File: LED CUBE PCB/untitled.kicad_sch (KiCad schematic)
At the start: 23 parts, among them J2 Conn_01x08, J4 Conn_01x04, SW2 RESET, U1 TPS7A2633DRVR, Y3 8MHz, Y4 32.786KHz

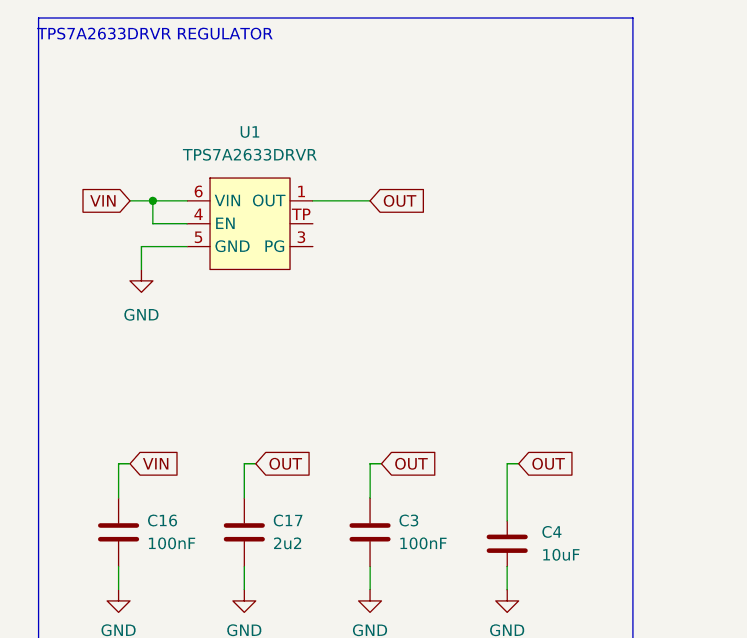
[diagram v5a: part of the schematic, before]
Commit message: Connected voltage regulator and logic level converter
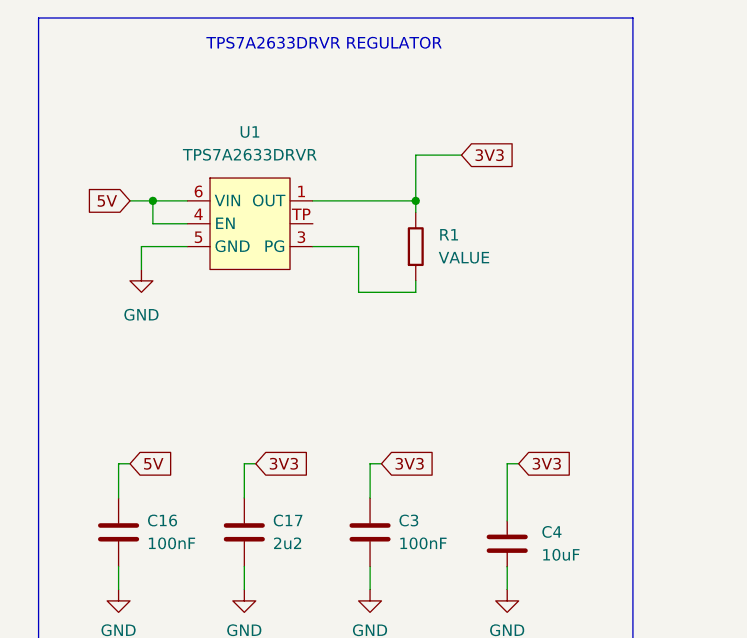
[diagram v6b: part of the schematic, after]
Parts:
- added R1: VALUE, Borna KiCAD Library:R0603, symbol Borna KiCAD Library:R0603
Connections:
- net 3V3: now also C17.1, C3.1, C4.2, U1.1 (OUT), R1.2
- net OUT: no longer C17.1, C3.1, C4.2, U1.1 (OUT)
- net at U1.3 (PG): now also R1.1
- net VIN renamed 5V
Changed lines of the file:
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@@
 	(text "TPS7A2633DRVR REGULATOR"
 		(exclude_from_sim no)
-		(at 26.924 14.732 0)
+		(at 45.72 15.748 0)
 		(effects
 			(font
@@
 	)
 	(junction
+		(at 55.88 33.02)
+		(diameter 0)
+		(color 0 0 0 0)
+	)
+	(junction
 		(at 153.67 140.97)
 		(diameter 0)
@@
 	(wire
 		(pts
+			(xy 55.88 43.18) (xy 55.88 41.91)
+		)
+		(stroke
+			(width 0)
+			(type default)
+		)
+	)
+	(wire
+		(pts
 			(xy 107.315 101.346) (xy 107.315 105.156)
 		)
@@
 	(wire
 		(pts
+			(xy 55.88 33.02) (xy 55.88 27.94)
+		)
+		(stroke
+			(width 0)
+			(type default)
+		)
+	)
+	(wire
+		(pts
 			(xy 130.81 99.06) (xy 148.59 99.06)
 		)
@@
 	(wire
 		(pts
+			(xy 49.53 43.18) (xy 55.88 43.18)
+		)
+		(stroke
+			(width 0)
+			(type default)
+		)
+	)
+	(wire
+		(pts
+			(xy 49.53 38.1) (xy 49.53 43.18)
+		)
+		(stroke
+			(width 0)
+			(type default)
+		)
+	)
+	(wire
+		(pts
 			(xy 247.65 29.21) (xy 264.16 29.21)
 		)
@@
 	(wire
 		(pts
+			(xy 55.88 33.02) (xy 55.88 34.29)
+		)
+		(stroke
+			(width 0)
+			(type default)
+		)
+	)
+	(wire
+		(pts
 			(xy 203.2 38.1) (xy 207.01 38.1)
 		)
@@
 	(wire
 		(pts
+			(xy 55.88 27.94) (xy 60.96 27.94)
+		)
+		(stroke
+			(width 0)
+			(type default)
+		)
+	)
+	(wire
+		(pts
 			(xy 247.65 62.23) (xy 250.19 62.23)
 		)
@@
 	(wire
 		(pts
-			(xy 44.45 33.02) (xy 50.8 33.02)
+			(xy 44.45 33.02) (xy 55.88 33.02)
 		)
 		(stroke
@@
 	(wire
 		(pts
+			(xy 44.45 38.1) (xy 49.53 38.1)
+		)
+		(stroke
+			(width 0)
+			(type default)
+		)
+	)
+	(wire
+		(pts
 			(xy 200.66 64.77) (xy 200.66 63.5)
 		)
@@
 		)
 	)
-	(global_label "OUT"
+	(global_label "3V3"
 		(shape input)
-		(at 50.8 33.02 0)
+		(at 60.96 27.94 0)
 		(fields_autoplaced yes)
 		(effects
@@
 		)
 		(property "Intersheetrefs" "${INTERSHEET_REFS}"
-			(at 57.4138 33.02 0)
+			(at 67.4528 27.94 0)
 			(effects
 				(font
@@
 		)
 	)
-	(global_label "OUT"
+	(global_label "3V3"
 		(shape input)
 		(at 67.31 62.23 0)
@@
 		)
 		(property "Intersheetrefs" "${INTERSHEET_REFS}"
-			(at 73.9238 62.23 0)
+			(at 73.8028 62.23 0)
 			(effects
 				(font
@@
 		)
 	)
-	(global_label "VIN"
+	(global_label "5V"
 		(shape input)
 		(at 24.13 33.02 180)
@@
 		)
 		(property "Intersheetrefs" "${INTERSHEET_REFS}"
-			(at 18.1209 33.02 0)
+			(at 18.8467 33.02 0)
 			(effects
 				(font
@@
 		)
 	)
-	(global_label "OUT"
+	(global_label "3V3"
 		(shape input)
 		(at 52.07 62.23 0)
@@
 		)
 		(property "Intersheetrefs" "${INTERSHEET_REFS}"
-			(at 58.6838 62.23 0)
+			(at 58.5628 62.23 0)
 			(effects
 				(font
@@
 		)
 	)
-	(global_label "VIN"
+	(global_label "5V"
 		(shape input)
 		(at 24.13 62.23 0)
@@
 		)
 		(property "Intersheetrefs" "${INTERSHEET_REFS}"
-			(at 30.1391 62.23 0)
+			(at 29.4133 62.23 0)
 			(effects
 				(font
@@
 		)
 	)
-	(global_label "OUT"
+	(global_label "3V3"
 		(shape input)
 		(at 38.1 62.23 0)
@@
 		)
 		(property "Intersheetrefs" "${INTERSHEET_REFS}"
-			(at 44.7138 62.23 0)
+			(at 44.5928 62.23 0)
 			(effects
 				(font
@@
 					(unit 1)
 				)
+			)
+		)
+	)
+	(symbol
+		(lib_id "Borna KiCAD Library:R0603")
+		(at 55.88 38.1 90)
+		(unit 1)
+		(exclude_from_sim no)
+		(in_bom yes)
+		(on_board yes)
+		(dnp no)
+		(fields_autoplaced yes)
+		(property "Reference" "R1"
+			(at 58.42 36.8299 90)
+			(effects
+				(font
+					(size 1.27 1.27)
+				)
+				(justify right)
+			)
+		)
+		(property "Value" "VALUE"
+			(at 58.42 39.3699 90)
+			(effects
+				(font
+					(size 1.27 1.27)
+				)
+				(justify right)
+			)
+		)
+		(property "Footprint" "Borna KiCAD Library:R0603"
+			(at 59.69 38.1 0)
+			(effects
+				(font
+					(size 1.27 1.27)
+				)
+				(hide yes)
+			)
+		)
+		(property "Datasheet" ""
+			(at 55.88 38.1 0)
+			(effects
+				(font
+					(size 1.27 1.27)
+				)
+				(hide yes)
+			)
+		)
+		(property "Description" ""
+			(at 55.88 38.1 0)
+			(effects
+				(font
+					(size 1.27 1.27)
+				)
+				(hide yes)
+			)
+		)
+		(pin "2"
+		)
+		(pin "1"
+		)
+		(instances
+			(project ""
+				(path "/64eb2d32-222b-4351-90b6-2cc90b760e62/ccca4637-6427-4f45-abce-b48cba1912e2"
+					(reference "R1")
+					(unit 1)
+				)

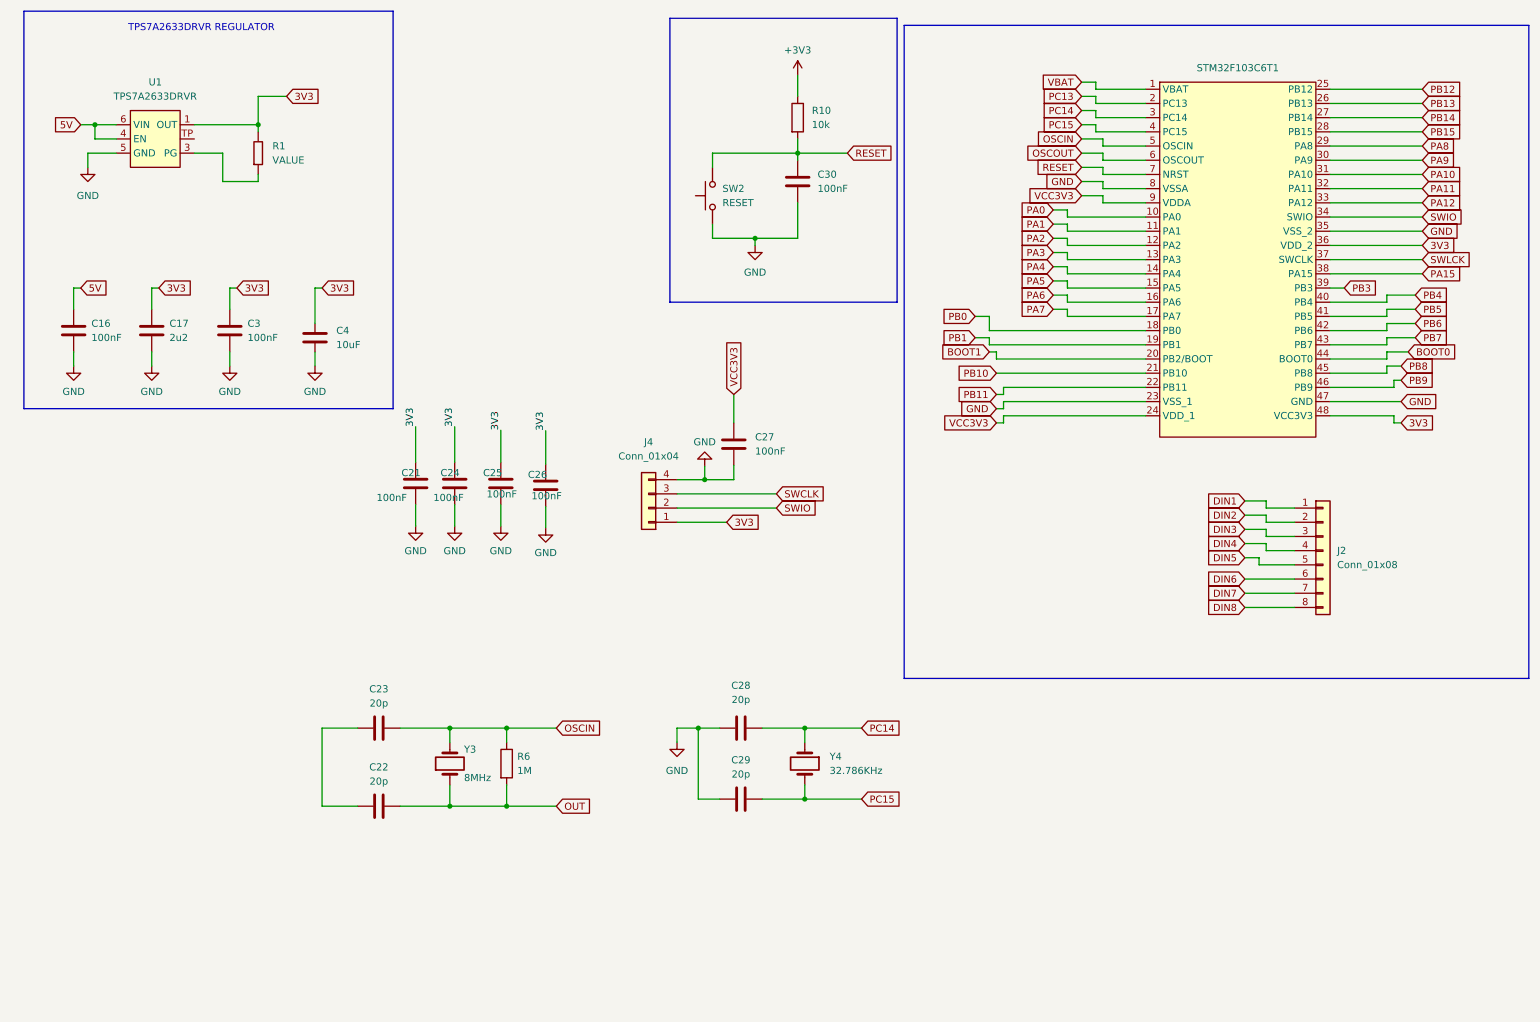
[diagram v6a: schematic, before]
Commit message: Added USB C and CH340C
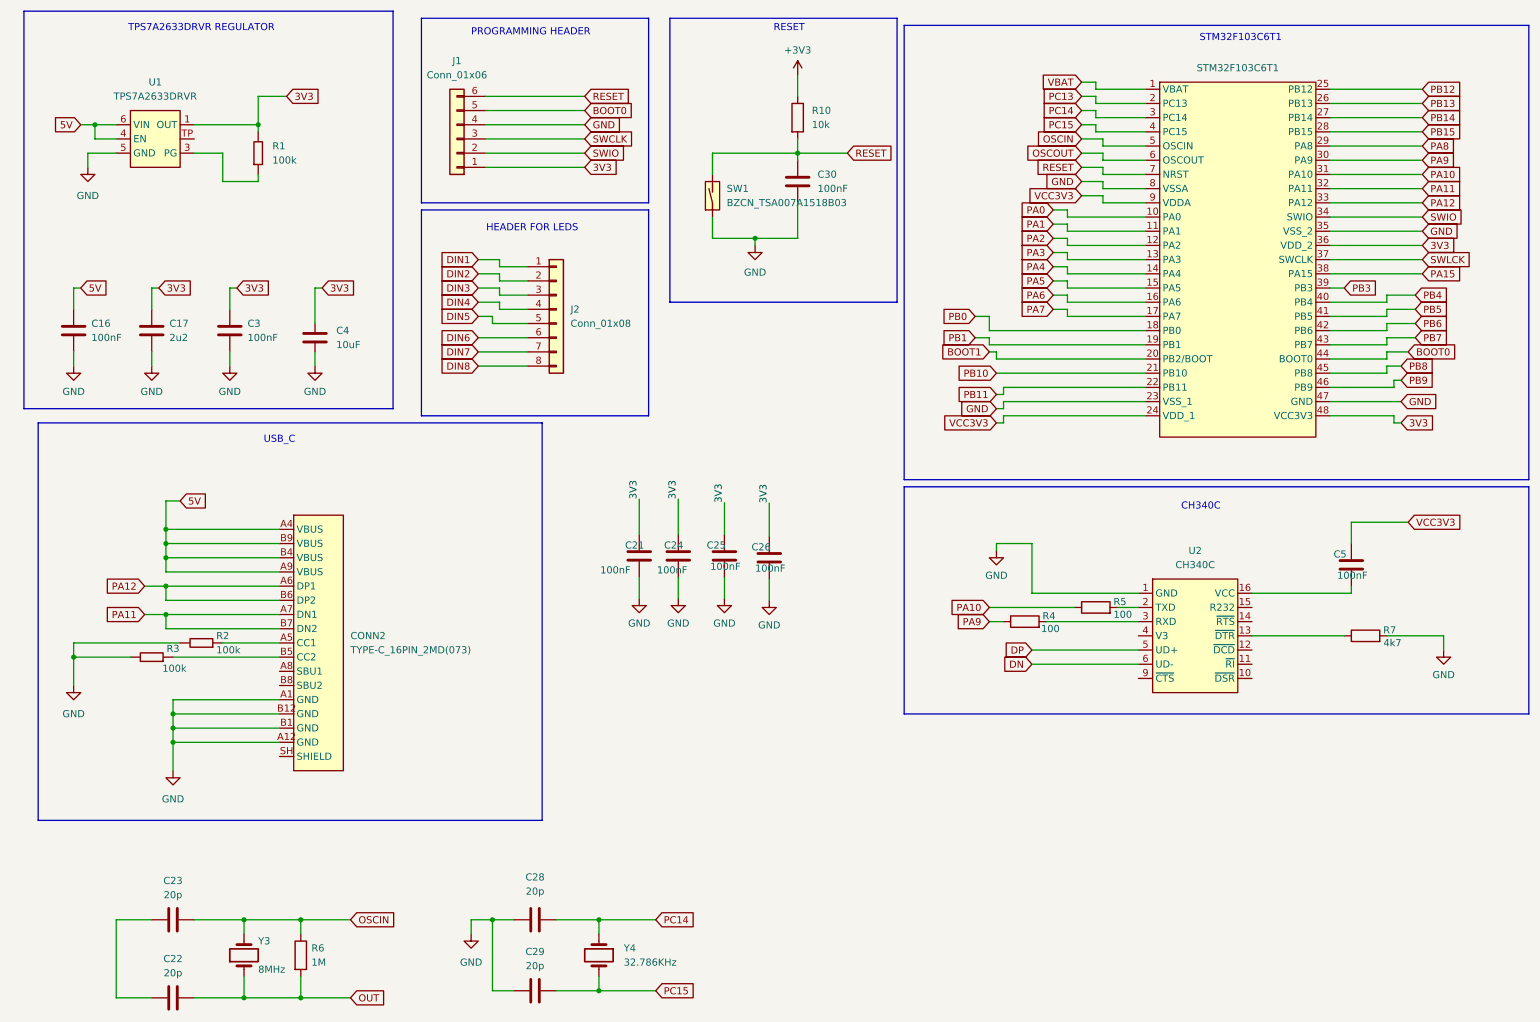
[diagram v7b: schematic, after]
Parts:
- removed C27: 100nF, Capacitor_SMD:C_0201_0603Metric, symbol Device:C
- removed J4: Conn_01x04, Connector_PinHeader_2.54mm:PinHeader_1x04_P2.54mm_Vertical, symbol Connector_Generic:Conn_01x04
- removed SW2: RESET, SMD_PUSH_BUTTON:SMD_BUTTON, symbol Switch:SW_Push
- added C5: 100nF, Borna KiCAD Library:C0603, symbol Device:C
- added CONN2: TYPE-C_16PIN_2MD(073), Borna KiCAD Library:TYPE-C_16PIN_2MD(073), symbol Borna KiCAD Library:TYPE-C_16PIN_2MD(073)
- added J1: Conn_01x06, Connector_PinHeader_2.54mm:PinHeader_1x06_P2.54mm_Vertical, symbol Connector_Generic:Conn_01x06
- added R2, R3: 100k, Borna KiCAD Library:R0603, symbol Borna KiCAD Library:R0603
- added R4, R5: 100, Resistor_SMD:R_0201_0603Metric, symbol Device:R
- added R7: 4k7, Resistor_SMD:R_0201_0603Metric, symbol Device:R
- added SW1: BZCN_TSA007A1518B03, Borna KiCAD Library:TSA007A1518B03, symbol Borna KiCAD Library:BZCN_TSA007A1518B03
- added U2: CH340C, Borna KiCAD Library:SOP-16, symbol Borna KiCAD Library:CH340C
- R1: value VALUE -> 100k
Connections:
- net 3V3: now also J1.1 (Pin_1)
- net 5V: now also CONN2.A4 (VBUS), CONN2.A9 (VBUS), CONN2.B4 (VBUS), CONN2.B9 (VBUS)
- net BOOT0: now also J1.5 (Pin_5)
- net GND: now also CONN2.A1 (GND), CONN2.A12 (GND), CONN2.B1 (GND), CONN2.B12 (GND), J1.4 (Pin_4), R2.2, R3.2, R7.2, SW1.1 (SW1), U2.1 (GND)
- net PA10: now also R5.1
- net PA11: now also CONN2.A7 (DN1), CONN2.B7 (DN2)
- net PA12: now also CONN2.A6 (DP1), CONN2.B6 (DP2)
- net PA9: now also R4.1
- net RESET: now also J1.6 (Pin_6), SW1.2 (SW2)
- net SWCLK: now also J1.3 (Pin_3)
- net SWIO: now also J1.2 (Pin_2)
- net VCC3V3: now also C5.1
- new net: R4.2, U2.3 (RXD)
- new net: R7.1, U2.13 (~{DTR})
- new net: C5.2, U2.16 (VCC)
- new net: R5.2, U2.2 (TXD)
- new net: CONN2.A5 (CC1), R2.1
- new net: CONN2.B5 (CC2), R3.1
- new net DN: U2.6 (UD-)
- new net DP: U2.5 (UD+)
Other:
- note added: "CH340C"
- note added: "HEADER FOR LEDS"
- note added: "PROGRAMMING HEADER"
- note added: "RESET"
- note added: "STM32F103C6T1"
- note added: "USB_C"
- moved on the sheet: C21, C22, C23, C24, C25, C26, C28, C29, J2, R6, Y3, Y4

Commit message: Corrected schema after review by Borna (Marina)
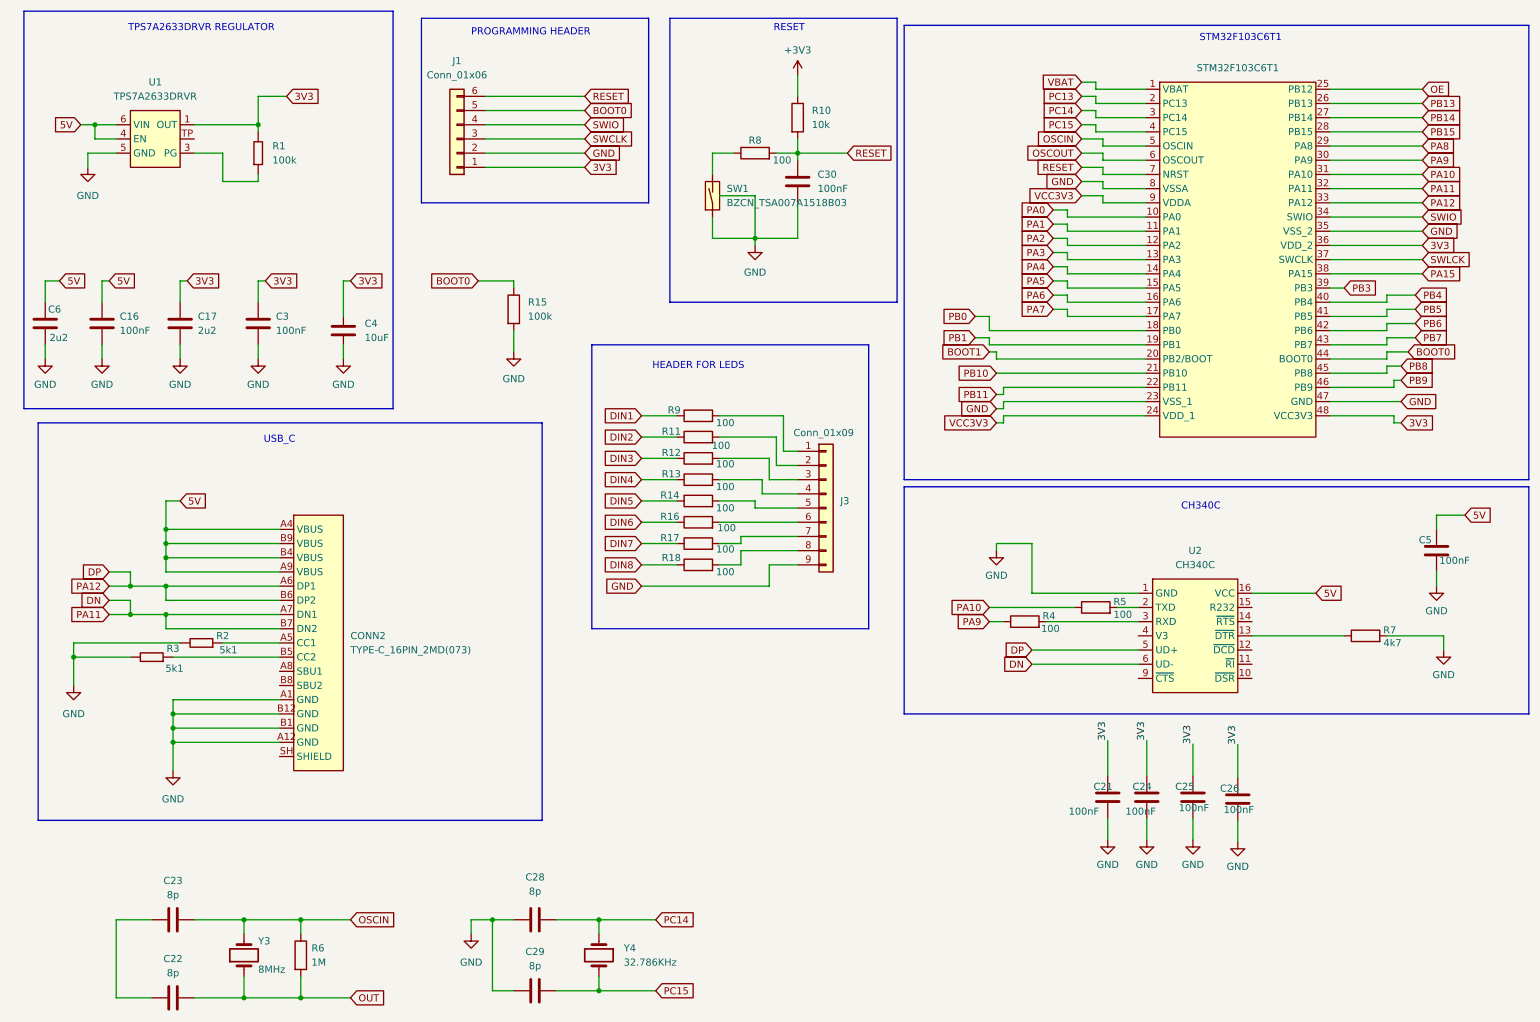
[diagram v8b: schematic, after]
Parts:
- removed J2: Conn_01x08, Connector_PinHeader_2.54mm:PinHeader_1x08_P2.54mm_Vertical, symbol Connector_Generic:Conn_01x08
- added C6: 2u2, BornaKiCad:C0603, symbol Device:C
- added J3: Conn_01x09, Connector_PinHeader_2.54mm:PinHeader_1x09_P2.54mm_Vertical, symbol Connector_Generic:Conn_01x09
- added R11, R12, R13, R14, R16, R17, R18, R8, R9: 100, BornaKiCad:R0603, symbol Device:R
- added R15: 100k, BornaKiCad:R0603, symbol Device:R
- C22, C23, C28, C29: value 20p -> 8p
- R2, R3: value 100k -> 5k1
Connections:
- net PA11 is gone; now on net DN: CONN2.A7 (DN1), CONN2.B7 (DN2), STM32F103C6T1.32 (PA11)
- net PA12 is gone; now on net DP: CONN2.A6 (DP1), CONN2.B6 (DP2), STM32F103C6T1.33 (PA12)
- net 5V: now also C5.1, U2.16 (VCC), C6.1
- net BOOT0: now also R15.1
- net DIN1: now also R9.1
- net DIN2: now also R11.1
- net DIN3: now also R12.1
- net DIN4: now also R13.1
- net DIN5: now also R14.1
- net DIN6: now also R16.1
- net DIN7: now also R17.1
- net DIN8: now also R18.1
- net GND: now also C5.2, J1.2 (Pin_2), SW1.PAD, C6.2, J3.9 (Pin_9), R15.2; no longer J1.4 (Pin_4)
- net RESET: now also R8.2; no longer SW1.2 (SW2)
- net SWIO: now also J1.4 (Pin_4); no longer J1.2 (Pin_2)
- net VCC3V3: no longer C5.1
- net PB12 renamed OE
- new net: J3.5 (Pin_5), R14.2
- new net: J3.2 (Pin_2), R11.2
- new net: J3.4 (Pin_4), R13.2
- new net: J3.3 (Pin_3), R12.2
- new net: J3.1 (Pin_1), R9.2
- new net: R8.1, SW1.2 (SW2)
- new net: J3.6 (Pin_6), R16.2
- new net: J3.7 (Pin_7), R17.2
- new net: J3.8 (Pin_8), R18.2
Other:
- moved on the sheet: C16, C17, C21, C24, C25, C26, C3, C4, C5
